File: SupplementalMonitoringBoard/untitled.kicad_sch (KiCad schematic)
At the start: 6 parts

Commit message: thing
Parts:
- C15, C16, C17, C18, C19, C20: footprint (none) -> Capacitor_SMD:C_0805_2012Metric
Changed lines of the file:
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@@
 			)
 		)
-		(property "Footprint" ""
+		(property "Footprint" "Capacitor_SMD:C_0805_2012Metric"
 			(at 127 100.33 0)
 			(effects
@@
 			)
 		)
-		(property "Footprint" ""
+		(property "Footprint" "Capacitor_SMD:C_0805_2012Metric"
 			(at 138.43 85.09 0)
 			(effects
@@
 			)
 		)
-		(property "Footprint" ""
+		(property "Footprint" "Capacitor_SMD:C_0805_2012Metric"
 			(at 132.08 100.33 0)
 			(effects
@@
 			)
 		)
-		(property "Footprint" ""
+		(property "Footprint" "Capacitor_SMD:C_0805_2012Metric"
 			(at 146.05 106.68 0)
 			(effects
@@
 			)
 		)
-		(property "Footprint" ""
+		(property "Footprint" "Capacitor_SMD:C_0805_2012Metric"
 			(at 139.7 106.68 0)
 			(effects
@@
 			)
 		)
-		(property "Footprint" ""
+		(property "Footprint" "Capacitor_SMD:C_0805_2012Metric"
 			(at 143.51 85.09 0)
 			(effects

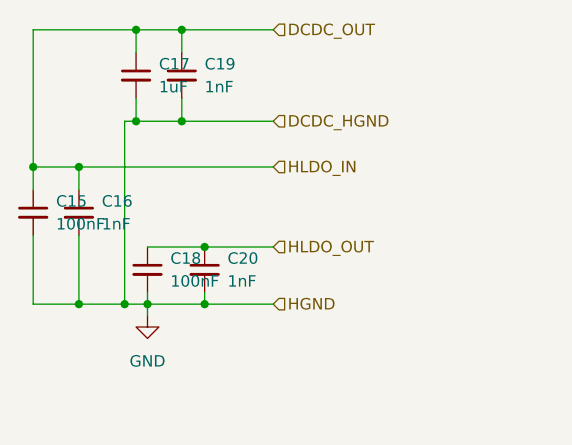
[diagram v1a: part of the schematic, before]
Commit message: Adressed Reviews - Supplemental Monitoring Board
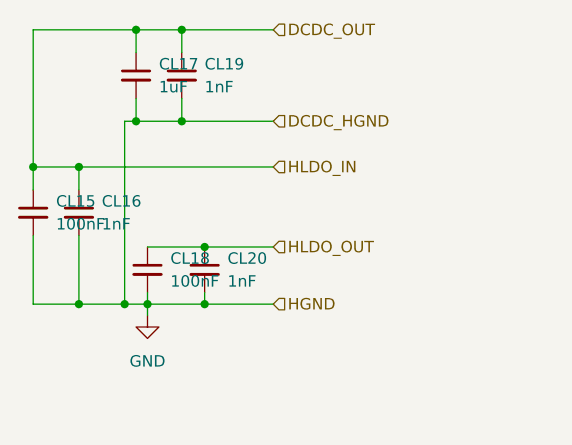
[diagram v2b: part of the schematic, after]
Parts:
- renumbered C15 to CL15, C16 to CL16, C17 to CL17, C18 to CL18, C19 to CL19, C20 to CL20
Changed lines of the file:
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@@
 		(dnp no)
 		(fields_autoplaced yes)
-		(property "Reference" "C15"
+		(property "Reference" "CL15"
 			(at 129.54 99.0662 0)
 			(effects
@@
 			(project "SupplementalMonitoringBoard"
 				(path "/aa0415d0-3287-4bc4-9a8e-766ada9ace2f/20ba7bd5-99e8-45e6-a6fa-f93b53aaa222"
-					(reference "C15")
+					(reference "CL15")
 					(unit 1)
 				)
@@
 		(dnp no)
 		(fields_autoplaced yes)
-		(property "Reference" "C17"
+		(property "Reference" "CL17"
 			(at 140.97 83.8262 0)
 			(effects
@@
 			(project "SupplementalMonitoringBoard"
 				(path "/aa0415d0-3287-4bc4-9a8e-766ada9ace2f/20ba7bd5-99e8-45e6-a6fa-f93b53aaa222"
-					(reference "C17")
+					(reference "CL17")
 					(unit 1)
 				)
@@
 		(dnp no)
 		(fields_autoplaced yes)
-		(property "Reference" "C16"
+		(property "Reference" "CL16"
 			(at 134.62 99.0662 0)
 			(effects
@@
 			(project "SupplementalMonitoringBoard"
 				(path "/aa0415d0-3287-4bc4-9a8e-766ada9ace2f/20ba7bd5-99e8-45e6-a6fa-f93b53aaa222"
-					(reference "C16")
+					(reference "CL16")
 					(unit 1)
 				)
@@
 		(dnp no)
 		(fields_autoplaced yes)
-		(property "Reference" "C20"
+		(property "Reference" "CL20"
 			(at 148.59 105.4162 0)
 			(effects
@@
 			(project "SupplementalMonitoringBoard"
 				(path "/aa0415d0-3287-4bc4-9a8e-766ada9ace2f/20ba7bd5-99e8-45e6-a6fa-f93b53aaa222"
-					(reference "C20")
+					(reference "CL20")
 					(unit 1)
 				)
@@
 		(dnp no)
 		(fields_autoplaced yes)
-		(property "Reference" "C18"
+		(property "Reference" "CL18"
 			(at 142.24 105.4162 0)
 			(effects
@@
 			(project "SupplementalMonitoringBoard"
 				(path "/aa0415d0-3287-4bc4-9a8e-766ada9ace2f/20ba7bd5-99e8-45e6-a6fa-f93b53aaa222"
-					(reference "C18")
+					(reference "CL18")
 					(unit 1)
 				)
@@
 		(dnp no)
 		(fields_autoplaced yes)
-		(property "Reference" "C19"
+		(property "Reference" "CL19"
 			(at 146.05 83.8262 0)
 			(effects
@@
 			(project "SupplementalMonitoringBoard"
 				(path "/aa0415d0-3287-4bc4-9a8e-766ada9ace2f/20ba7bd5-99e8-45e6-a6fa-f93b53aaa222"
-					(reference "C19")
-					(unit 1)
-				)
+					(reference "CL19")
+					(unit 1)
+				)
